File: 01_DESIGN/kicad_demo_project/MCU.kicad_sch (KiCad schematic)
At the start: 35 parts, among them J2 0473460001, J3 JP8, U3 STM32H745ZIT3, Y1 ECS-250-12-33Q-JES-TR

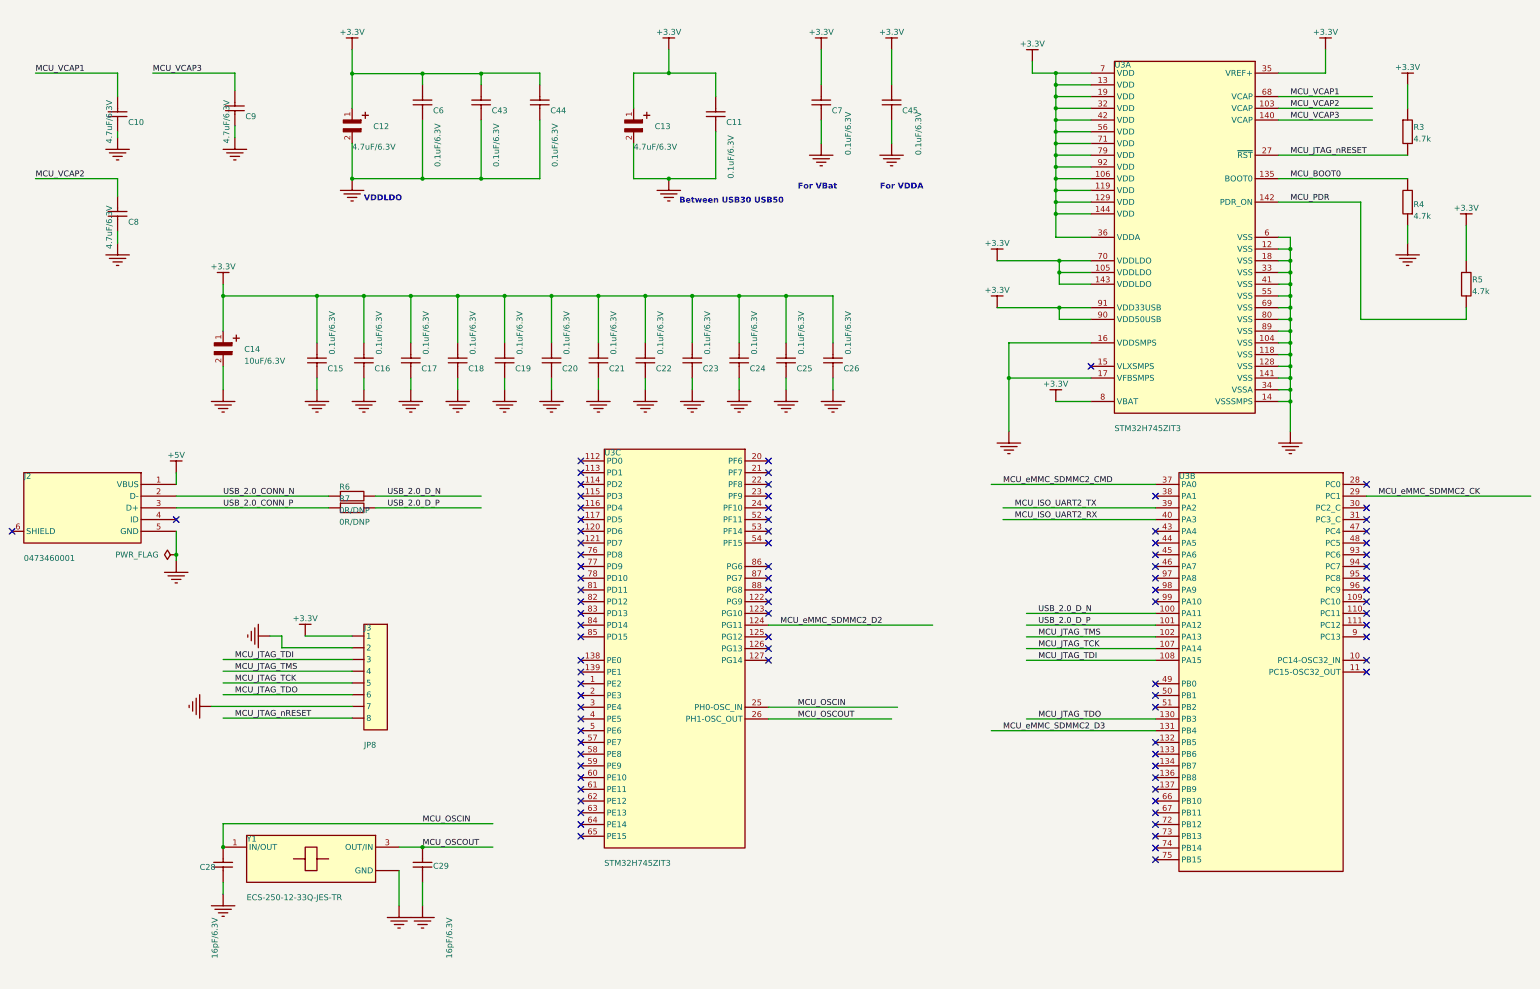
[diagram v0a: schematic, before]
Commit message: Update schematic, PCB
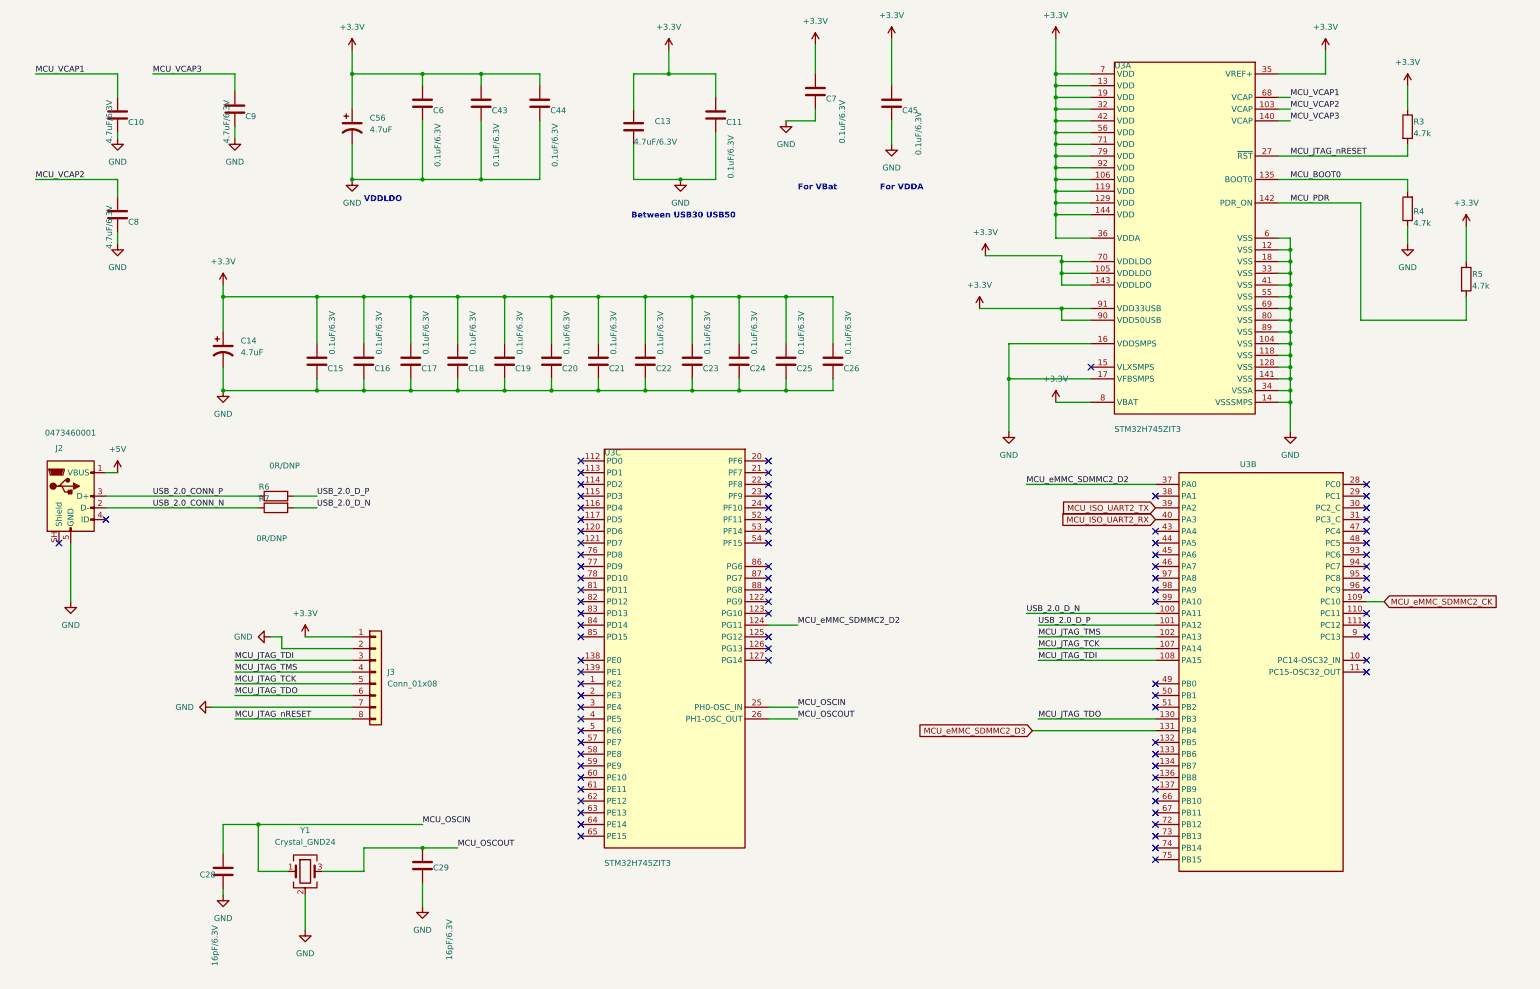
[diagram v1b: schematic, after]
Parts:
- removed C12: 4.7uF/6.3V, CAP_MP_1608X90, symbol TACL335M003RTA:root_1_mirrored_TACL335M003RTA_TACL335M003RTA.IntLib
- removed C14: 10uF/6.3V, CAP_MP_2012X170, symbol TACR686M003RTA:root_1_mirrored_TACR686M003RTA_TACR686M003RTA.IntLib
- removed J3: JP8, Connector_PinHeader_2.54mm:PinHeader_1x08_P2.54mm_Horizontal, symbol obc_ver2:root_0_JP8_obc_ver2.SCHLIB
- removed Y1: ECS-250-12-33Q-JES-TR, Package_QFP:LQFP-144_20x20mm_P0.5mm, symbol ECS-250-12-33Q-JES-TR:root_0_ECS-250-12-33Q-JES-TR_ECS-250-12-33Q-JES-TR.IntLib
- added C14, C56: 4.7uF, Capacitor_Tantalum_SMD:CP_EIA-2012-15_AVX-P, symbol Device:C_Polarized_US
- added J3: Conn_01x08, Connector_PinHeader_2.54mm:PinHeader_1x08_P2.54mm_Vertical, symbol Connector_Generic:Conn_01x08
- added Y1: Crystal_GND24, Crystal:Crystal_SMD_3225-4Pin_3.2x2.5mm, symbol Device:Crystal_GND24
- C10, C11, C15, C16, C17, C18, C19, C20, C21, C22, C23, C24, C25, C26, C44, C45, C6, C7, C8, C9: footprint CAP_C_1608X80 -> Capacitor_SMD:C_0603_1608Metric; symbol Altium_Lib_by_KhueNguyenCreator:root_1_Tu 0402 33nF 10V_Altium_Lib_by_KhueNguyenCreator.IntLib -> Device:C
- C13: footprint CAP_MP_1608X90 -> Capacitor_SMD:C_0603_1608Metric; symbol TACL335M003RTA:root_1_mirrored_TACL335M003RTA_TACL335M003RTA.IntLib -> Device:C
- C28, C29: footprint CAP_C_1608X80 -> Capacitor_SMD:C_0603_1608Metric; symbol Altium_Lib_by_KhueNguyenCreator:root_3_mirrored_Tu 0402 33nF 10V_Altium_Lib_by_KhueNguyenCreator.IntLib -> Device:C
- C43: footprint CAP_C_1608X80 -> Capacitor_SMD:CAP_C_1608X80; symbol Altium_Lib_by_KhueNguyenCreator:root_1_Tu 0402 33nF 10V_Altium_Lib_by_KhueNguyenCreator.IntLib -> Device:C
- J2: symbol obc_ver2:root_0_mirrored_USB_micro_obc_ver2.SCHLIB -> Connector:USB_B_Micro
- R3, R5: footprint RES_C_1608X60 -> Resistor_SMD:R_0603_1608Metric; symbol Altium_Lib_by_KhueNguyenCreator:root_3_Tro 0603 1% 10k_Altium_Lib_by_KhueNguyenCreator.IntLib -> Device:R
- R4: footprint RES_C_1608X60 -> Resistor_SMD:R_0603_1608Metric; symbol Altium_Lib_by_KhueNguyenCreator:root_1_Tro 0603 1% 10k_Altium_Lib_by_KhueNguyenCreator.IntLib -> Device:R
- R6, R7: footprint RES_C_1608X60 -> Resistor_SMD:R_0603_1608Metric; symbol Altium_Lib_by_KhueNguyenCreator:root_2_mirrored_Tro 0603 1% 1k_Altium_Lib_by_KhueNguyenCreator.IntLib -> Device:R
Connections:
- net MCU_eMMC_SDMMC2_CMD is gone; now on net MCU_eMMC_SDMMC2_D2: U3.37 (PA0)
- net +3.3V: now also C11.2, C13.2, C15.2, C16.2, C17.2, C18.2, C19.2, C20.2, C21.2, C22.2, C23.2, C24.2, C25.2, C26.2, C43.2, C44.2, C45.2, C6.2, C7.2, C14.1, C56.1, J3.1 (Pin_1); no longer C11.1, C13.1, C15.1, C16.1, C17.1, C18.1, C19.1, C20.1, C21.1, C22.1, C23.1, C24.1, C25.1, C26.1, C43.1, C44.1, C45.1, C6.1, C7.1
- net GND: now also C10.1, C11.1, C13.1, C15.1, C16.1, C17.1, C18.1, C19.1, C20.1, C21.1, C22.1, C23.1, C24.1, C25.1, C26.1, C28.2, C29.2, C43.1, C44.1, C45.1, C6.1, C7.1, C8.1, C9.1, C14.2, C56.2, J3.2 (Pin_2), J3.7 (Pin_7), Y1.2 (G), Y1.4 (G); no longer C10.2, C11.2, C13.2, C15.2, C16.2, C17.2, C18.2, C19.2, C20.2, C21.2, C22.2, C23.2, C24.2, C25.2, C26.2, C28.1, C29.1, C43.2, C44.2, C45.2, C6.2, C7.2, C8.2, C9.2
- net MCU_JTAG_TCK: now also J3.5 (Pin_5)
- net MCU_JTAG_TDI: now also J3.3 (Pin_3)
- net MCU_JTAG_TDO: now also J3.6 (Pin_6)
- net MCU_JTAG_TMS: now also J3.4 (Pin_4)
- net MCU_JTAG_nRESET: now also J3.8 (Pin_8)
- net MCU_OSCIN: now also C28.1, Y1.1; no longer C28.2
- net MCU_OSCOUT: now also C29.1, Y1.3; no longer C29.2
- net MCU_VCAP1: now also C10.2; no longer C10.1
- net MCU_VCAP2: now also C8.2; no longer C8.1
- net MCU_VCAP3: now also C9.2; no longer C9.1
- net MCU_eMMC_SDMMC2_CK: now also U3.109 (PC10); no longer U3.29 (PC1)
- net USB_2.0_CONN_N: now also R7.1; no longer R6.1
- net USB_2.0_CONN_P: now also R6.1; no longer R7.1
- net USB_2.0_D_N: now also R7.2; no longer R6.2
- net USB_2.0_D_P: now also R6.2; no longer R7.2
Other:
- moved on the sheet: R3, R4, R5, R6, R7
